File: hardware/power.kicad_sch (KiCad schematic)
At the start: 0 parts

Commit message: cleaned up serializer with comments and project hierarchy
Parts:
- added C14, C6, C9: 10U, Capacitor_SMD:C_0402_1005Metric, symbol Device:C
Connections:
- new net GND: C14.2, C6.2, C9.2

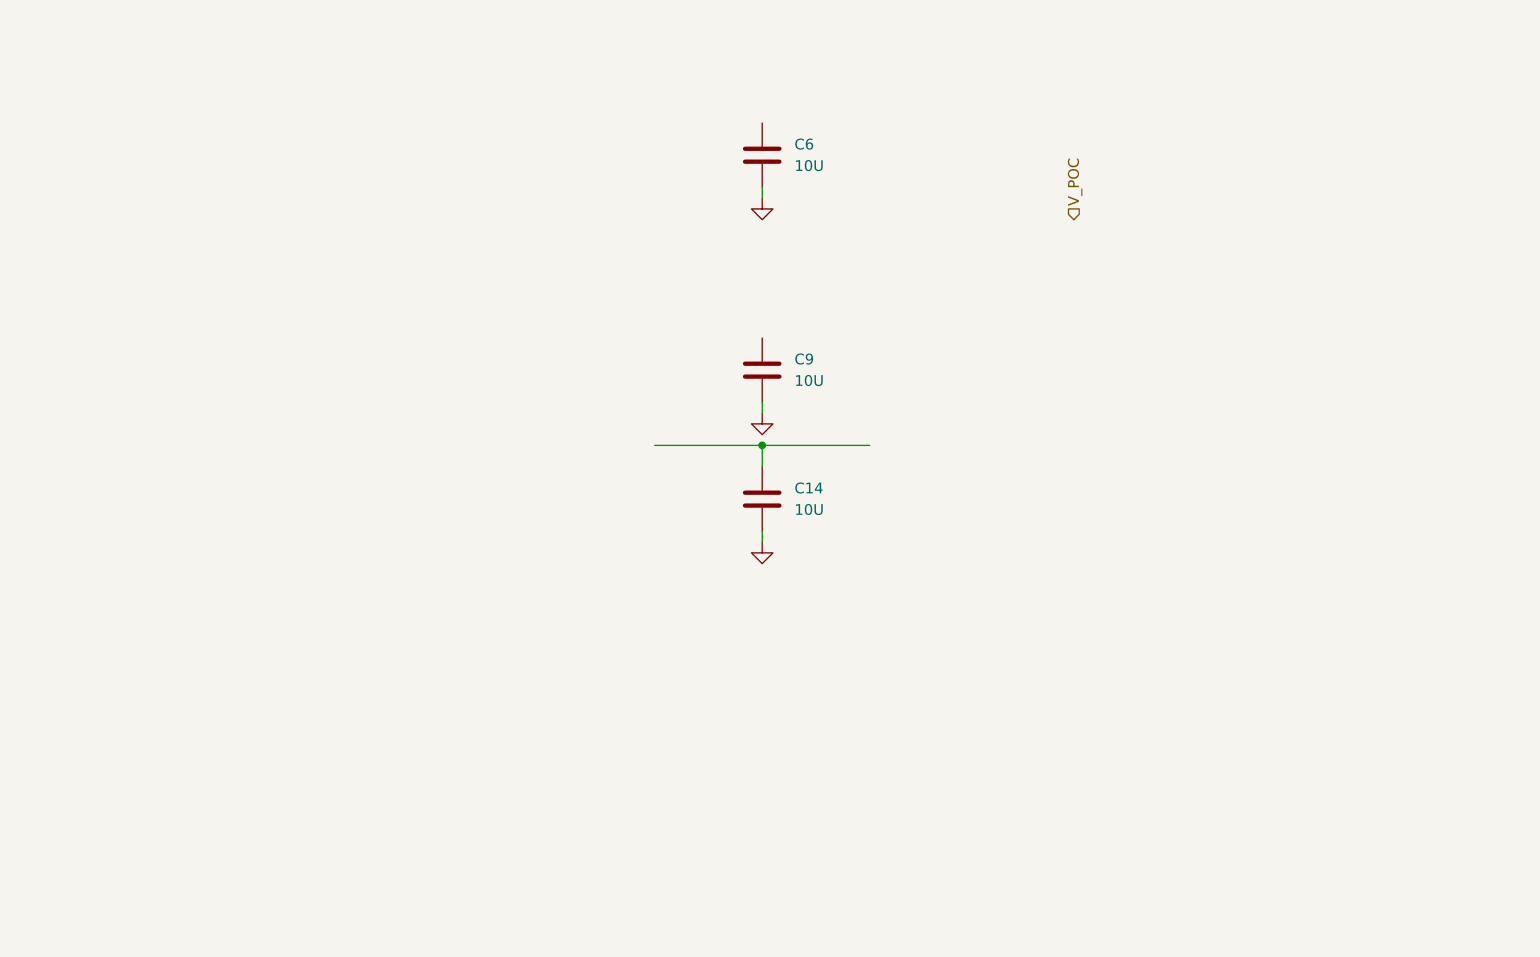
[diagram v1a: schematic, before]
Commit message: started power, added smt fakra
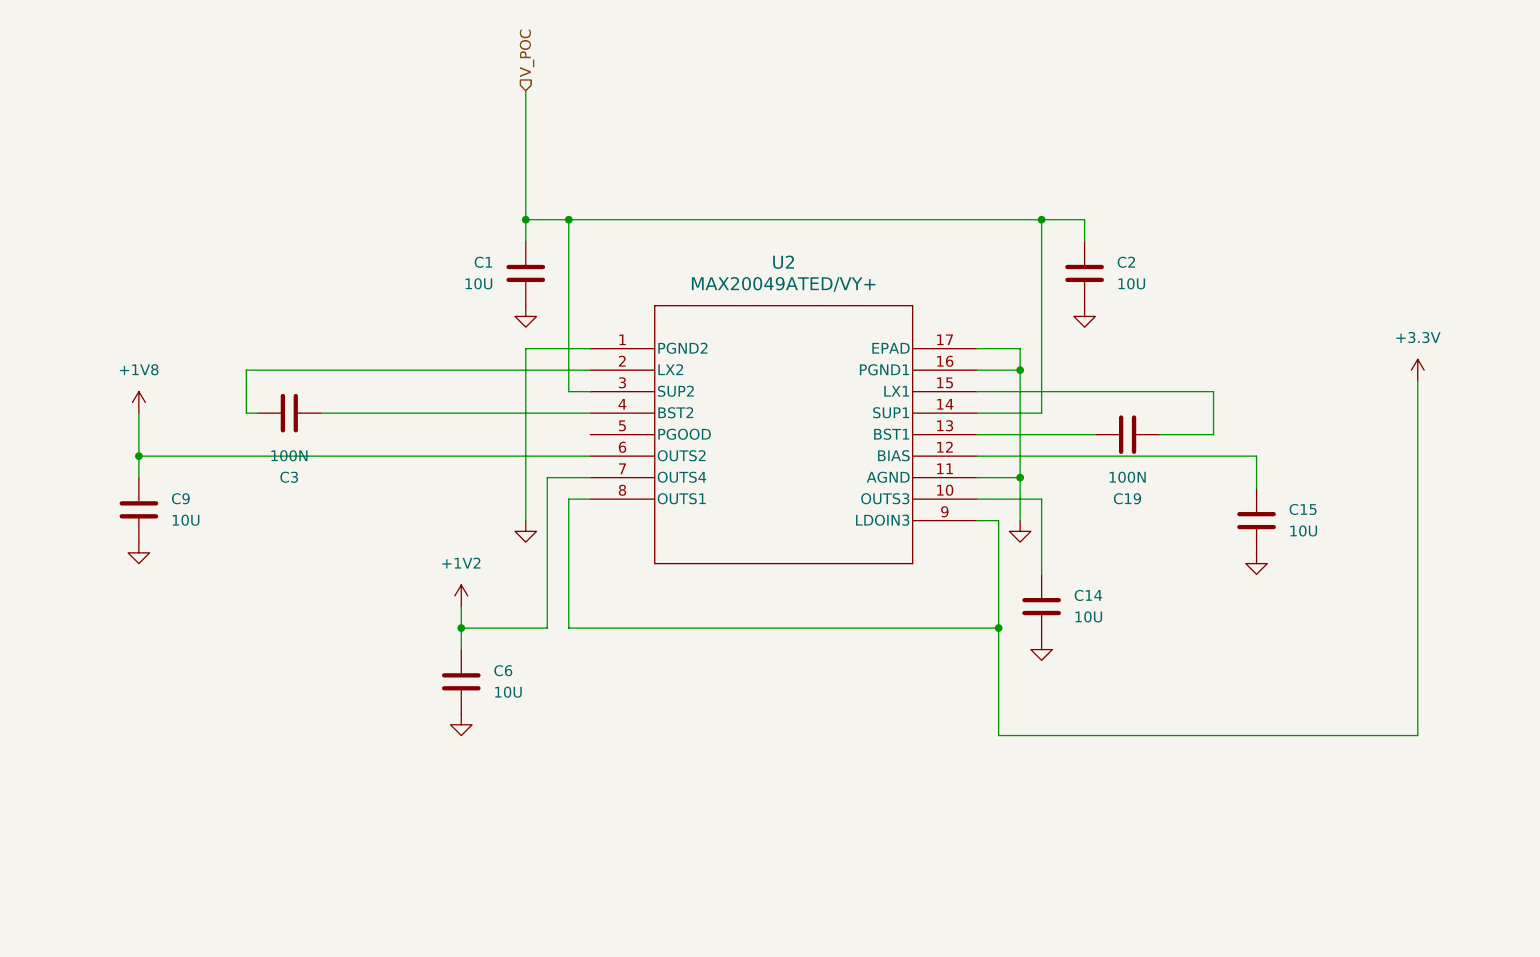
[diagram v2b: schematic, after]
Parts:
- added C1, C15, C2: 10U, Capacitor_SMD:C_0603_1608Metric, symbol Device:C
- added C19, C3: 100N, Capacitor_SMD:C_0402_1005Metric, symbol Device:C
- added U2: MAX20049ATED/VY+, user:21-100150D_T1633Y&plus_5C_MXM, symbol user:MAX20049ATED_VY+
- C14, C6, C9: footprint Capacitor_SMD:C_0402_1005Metric -> Capacitor_SMD:C_0603_1608Metric
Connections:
- net GND: now also C1.2, C15.2, C2.2, U2.1 (PGND2), U2.11 (AGND), U2.16 (PGND1), U2.17 (EPAD)
- net V_POC: now also C1.1, C2.1, U2.14 (SUP1), U2.3 (SUP2)
- net at C14.1: now also U2.10 (OUTS3)
- net +1V2: now reaches C6.1
- net +1V2: now also U2.7 (OUTS4)
- net +1V8: now reaches C9.1
- net +1V8: now also U2.6 (OUTS2)
- new net: C15.1, U2.12 (BIAS)
- new net: C19.1, U2.13 (BST1)
- new net: C19.2, U2.15 (LX1)
- new net: C3.1, U2.2 (LX2)
- new net: C3.2, U2.4 (BST2)
- new net +3.3V: U2.8 (OUTS1), U2.9 (LDOIN3)

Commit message: finished schematic, changed to 4 layer board
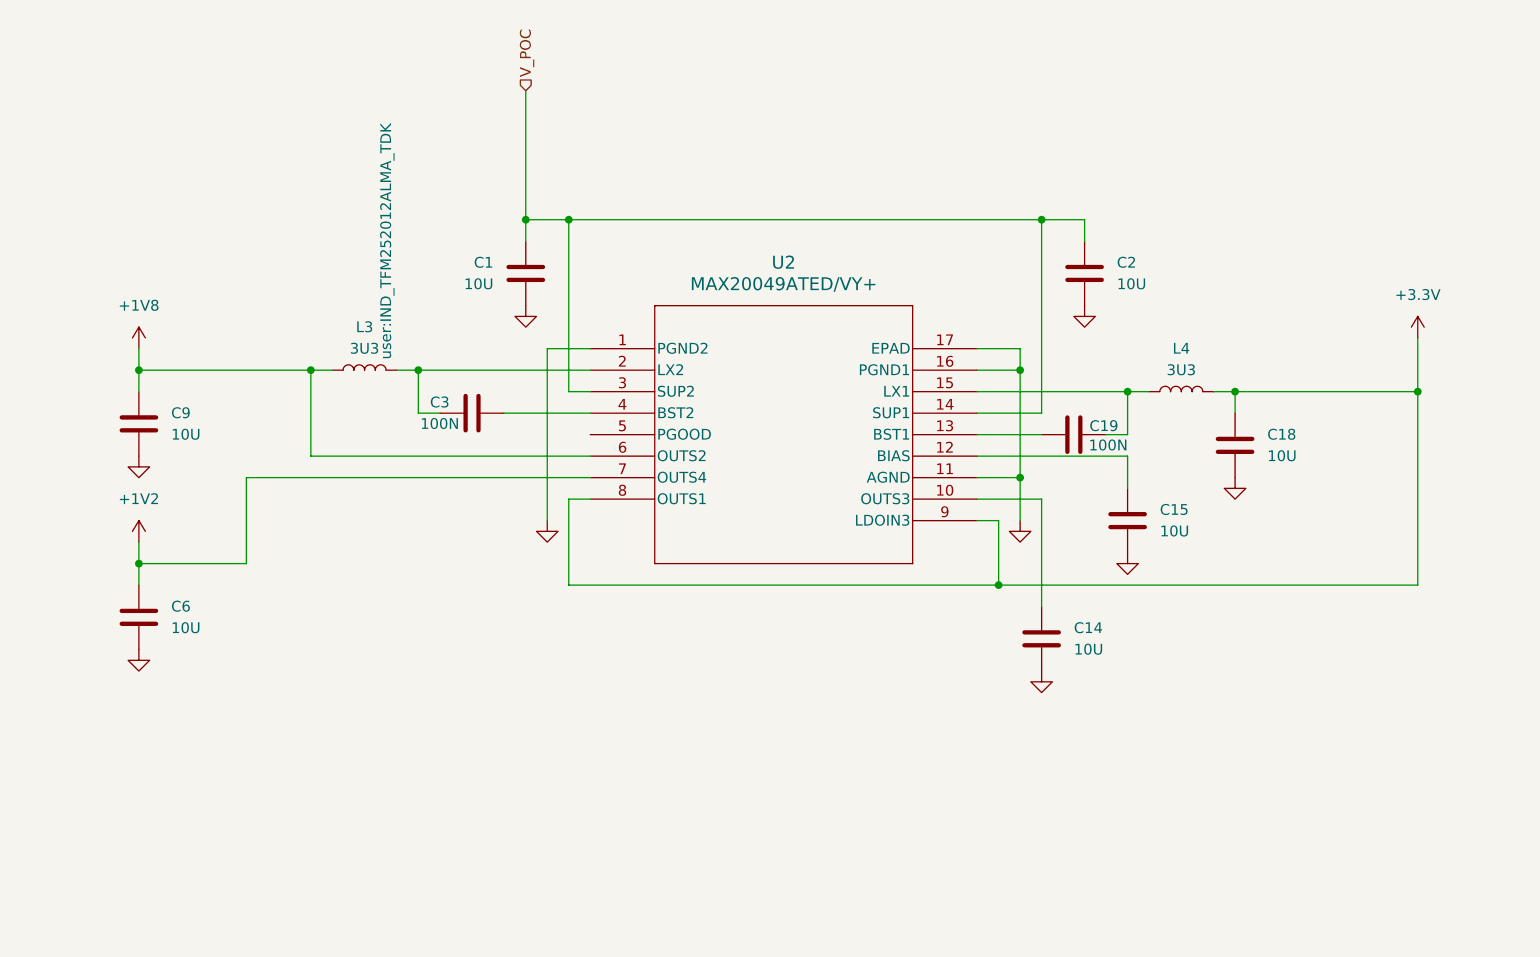
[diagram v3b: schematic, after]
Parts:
- added C18: 10U, Capacitor_SMD:C_0603_1608Metric, symbol Device:C
- added L3, L4: 3U3, user:IND_TFM252012ALMA_TDK, symbol user:TFM252012ALMA3R3MTAA
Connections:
- net +1V8: now also L3.1
- net +3.3V: now also C18.1, L4.2
- net GND: now also C18.2
- net at C19.2, U2.15 (LX1): now also L4.1
- net at C3.1, U2.2 (LX2): now also L3.2
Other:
- moved on the sheet: C14, C15, C19, C3, C6, C9

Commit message: layout planning and decided to use bottom layer for components
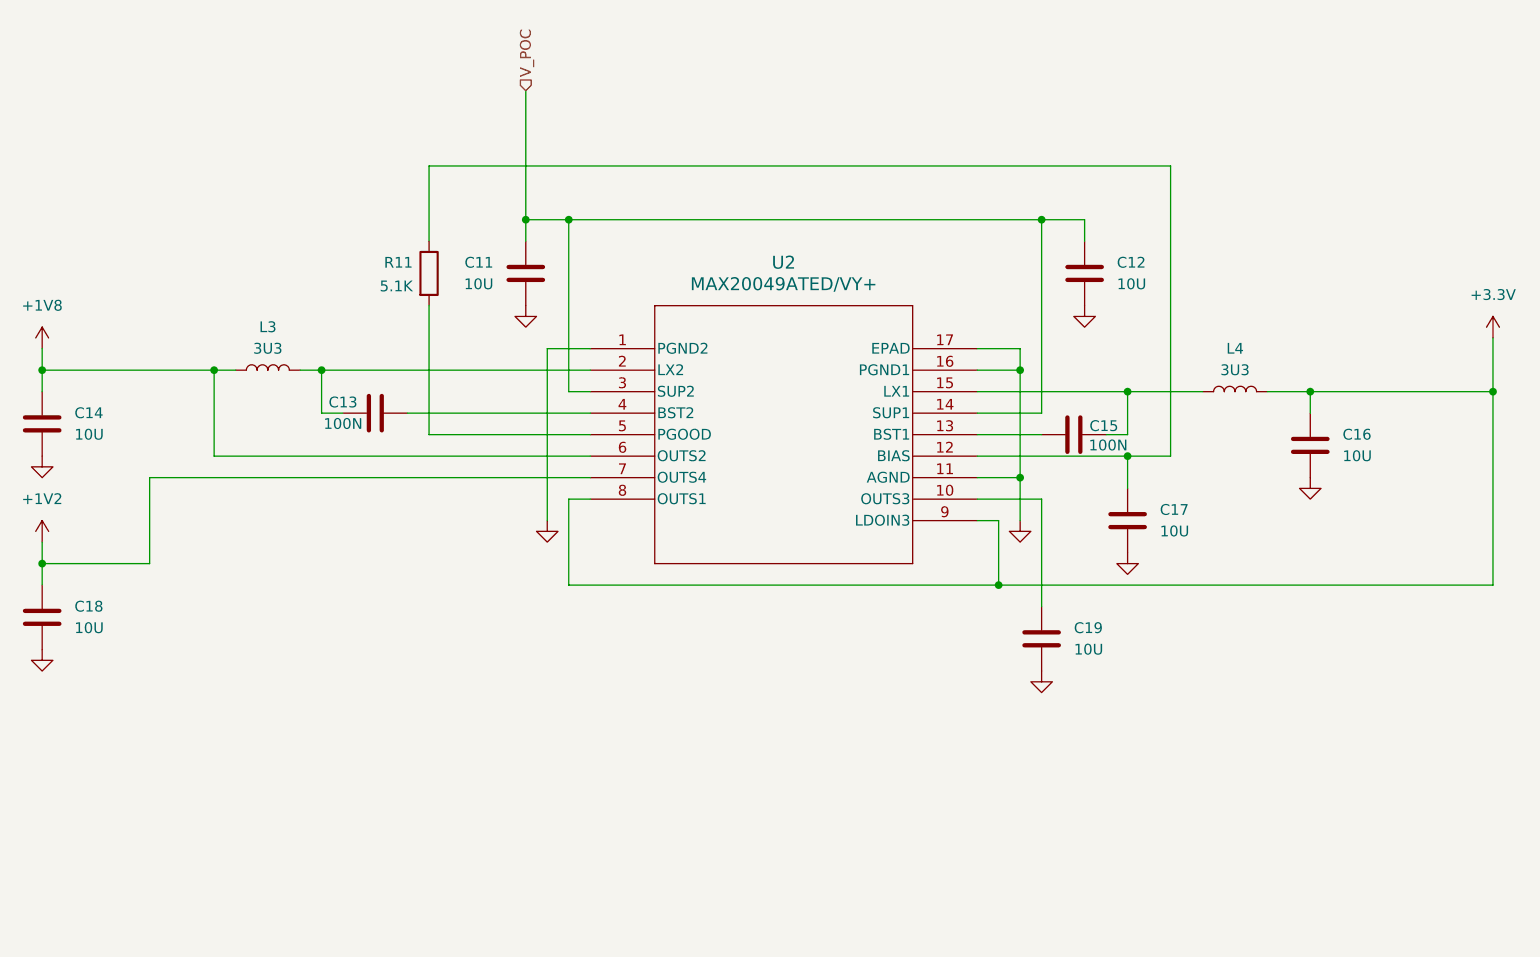
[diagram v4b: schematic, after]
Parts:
- added R11: 5.1K, Resistor_SMD:R_0402_1005Metric, symbol Device:R
- renumbered C1 to C11, C2 to C12, C3 to C13, C9 to C14, C19 to C15, C18 to C16, C15 to C17, C6 to C18, C14 to C19
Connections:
- net at C17.1, U2.12 (BIAS): now also R11.1
- net at U2.5 (PGOOD): now also R11.2
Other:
- moved on the sheet: C13, C14, C16, C18, L3, L4

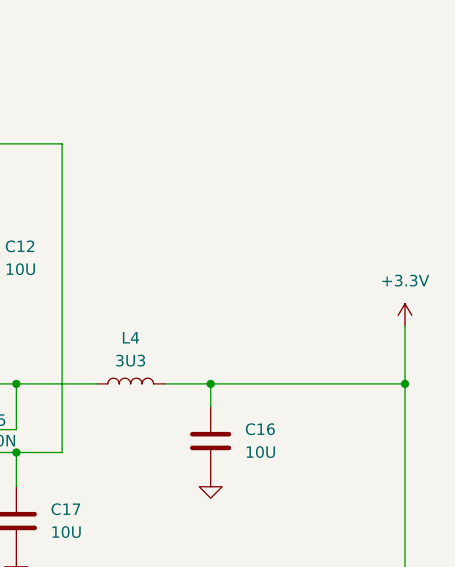
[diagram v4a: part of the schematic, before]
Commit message: cleaned up power supply and started minor power plane routing
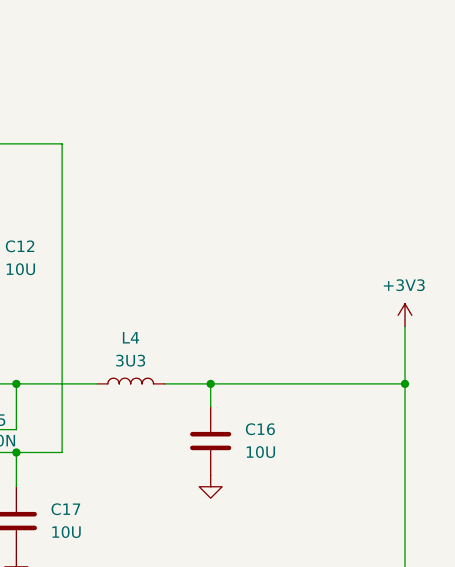
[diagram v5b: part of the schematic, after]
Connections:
- net +3.3V renamed +3V3
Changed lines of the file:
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@@
 		(on_board yes)
 		(dnp no)
-		(fields_autoplaced yes)
 		(property "Reference" "#PWR029"
 			(at 210.82 83.82 0)
@@
 			)
 		)
-		(property "Value" "+3.3V"
-			(at 210.82 74.93 0)
+		(property "Value" "+3V3"
+			(at 208.28 75.438 0)
 			(effects
 				(font
 					(size 1.27 1.27)
 				)
+				(justify left)
 			)
 		)

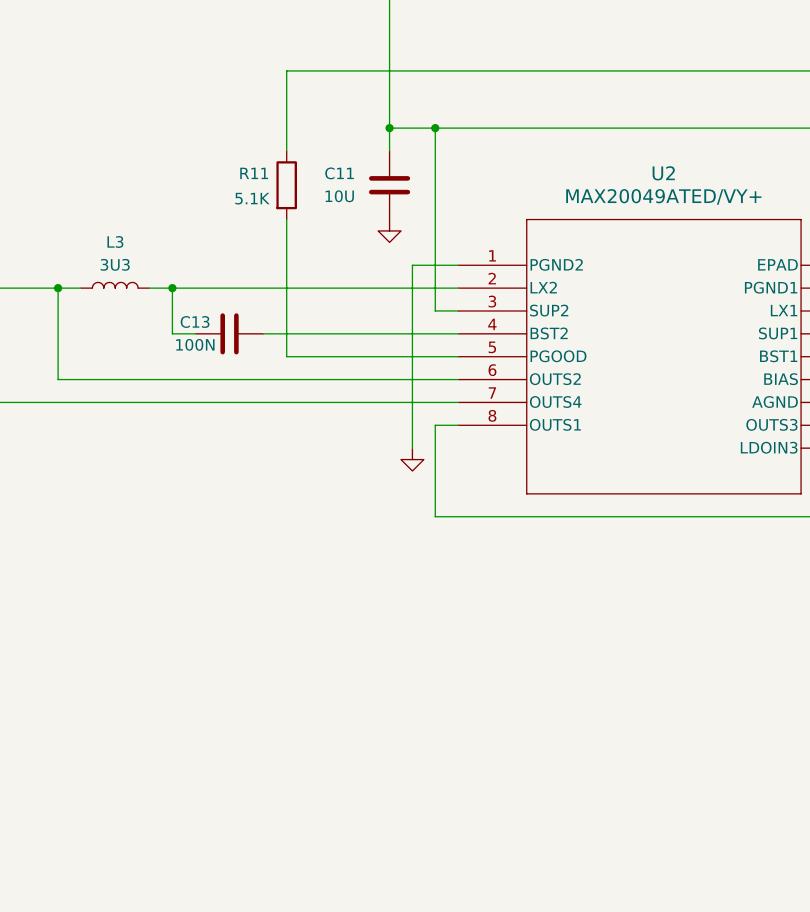
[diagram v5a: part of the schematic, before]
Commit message: added LED circuits and test points on extra MFPs
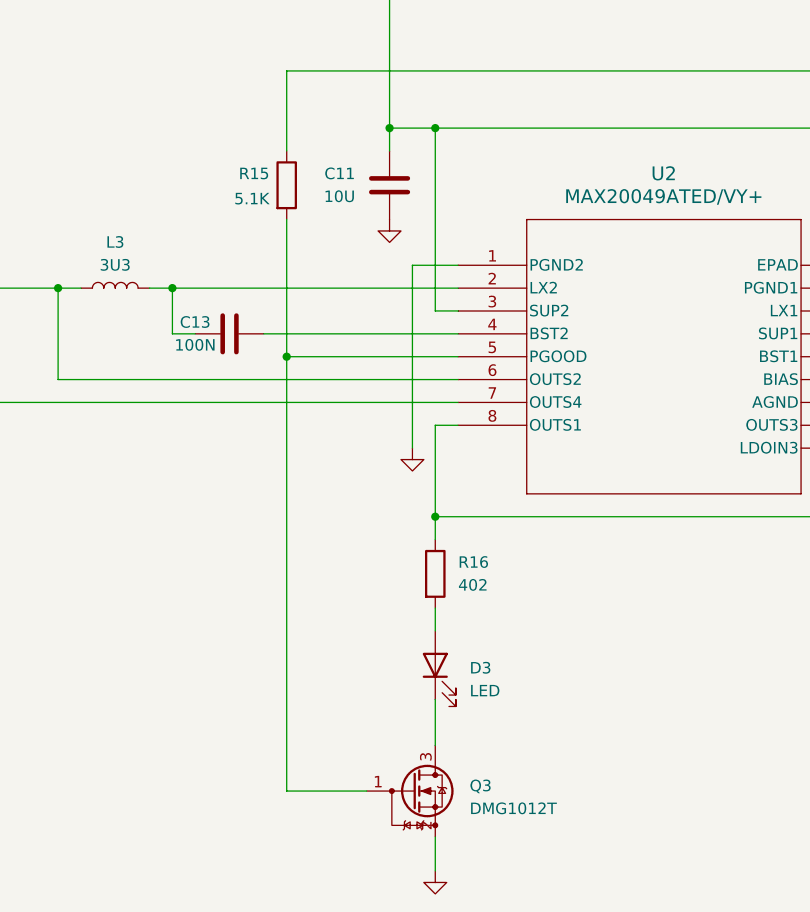
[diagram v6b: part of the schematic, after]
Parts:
- added D3: LED, LED_SMD:LED_0603_1608Metric, symbol Device:LED
- added Q3: DMG1012T, Package_TO_SOT_SMD:SOT-523, symbol Transistor_FET:DMG1012T
- added R16: 402, Resistor_SMD:R_0402_1005Metric, symbol Device:R
- renumbered R11 to R15
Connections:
- net +3V3: now also R16.1
- net GND: now also Q3.2 (S)
- net at R15.2, U2.5 (PGOOD): now also Q3.1 (G)
- new net: D3.1 (K), Q3.3 (D)
- new net: D3.2 (A), R16.2
